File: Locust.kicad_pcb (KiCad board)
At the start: 2 copper layers, 133.3 x 44.4 mm, 12 parts, among them J1 Conn_01x03_MountingPin, J2 Conn_01x03_MountingPin, J3 Conn_01x03_MountingPin, J4 Conn_01x06_MountingPin, J5 Conn_01x12_MountingPin, J6 Conn_01x05_MountingPin, U1 DRV8847RTE, U2 DRV8847RTE, U3 nRF7002-QFXX, U4 ISP2053-AX, U5 AP63203WU, U6 AP63205WU

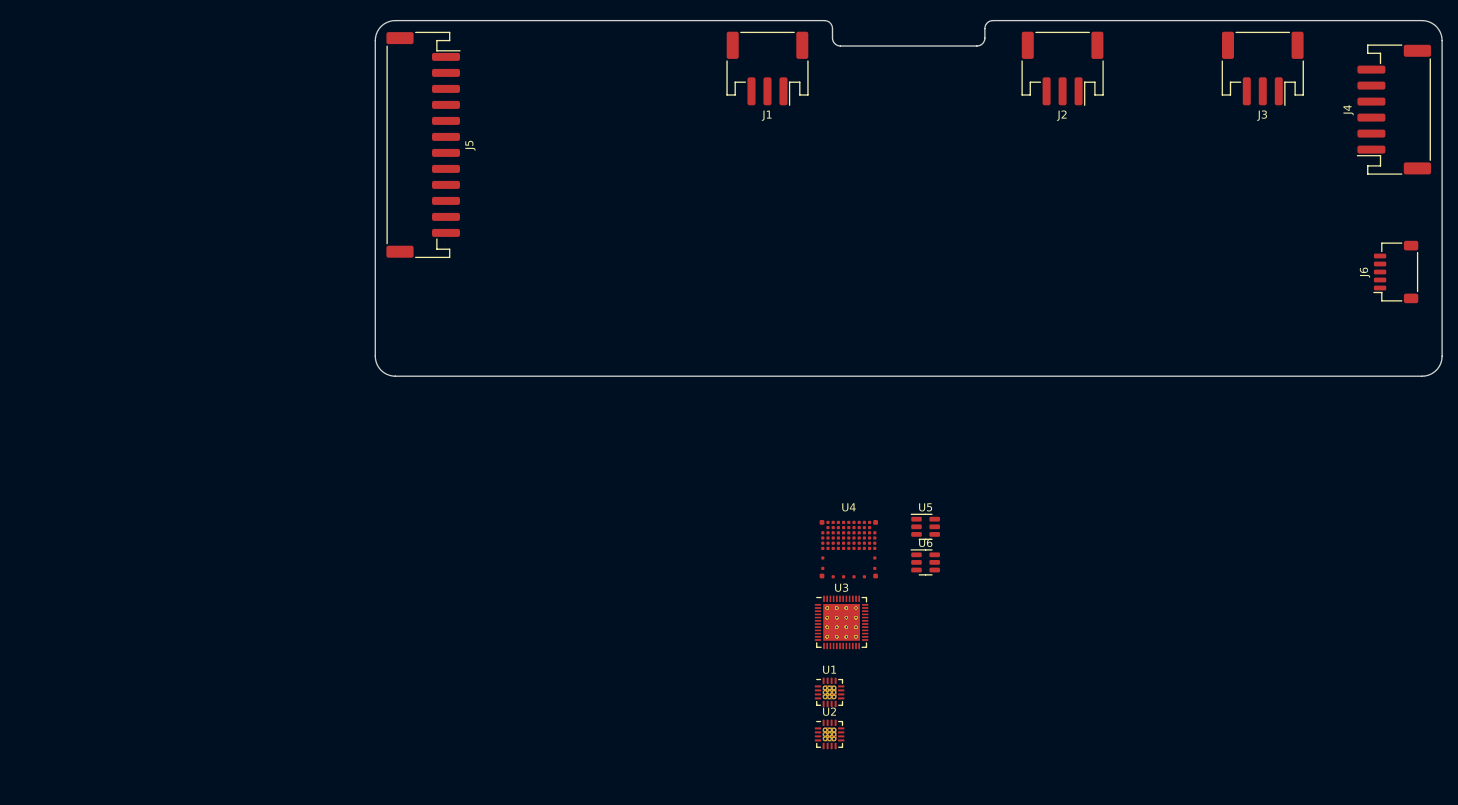
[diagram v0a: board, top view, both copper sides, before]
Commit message: Added nrf5340 and pi filters on output of switching supplies
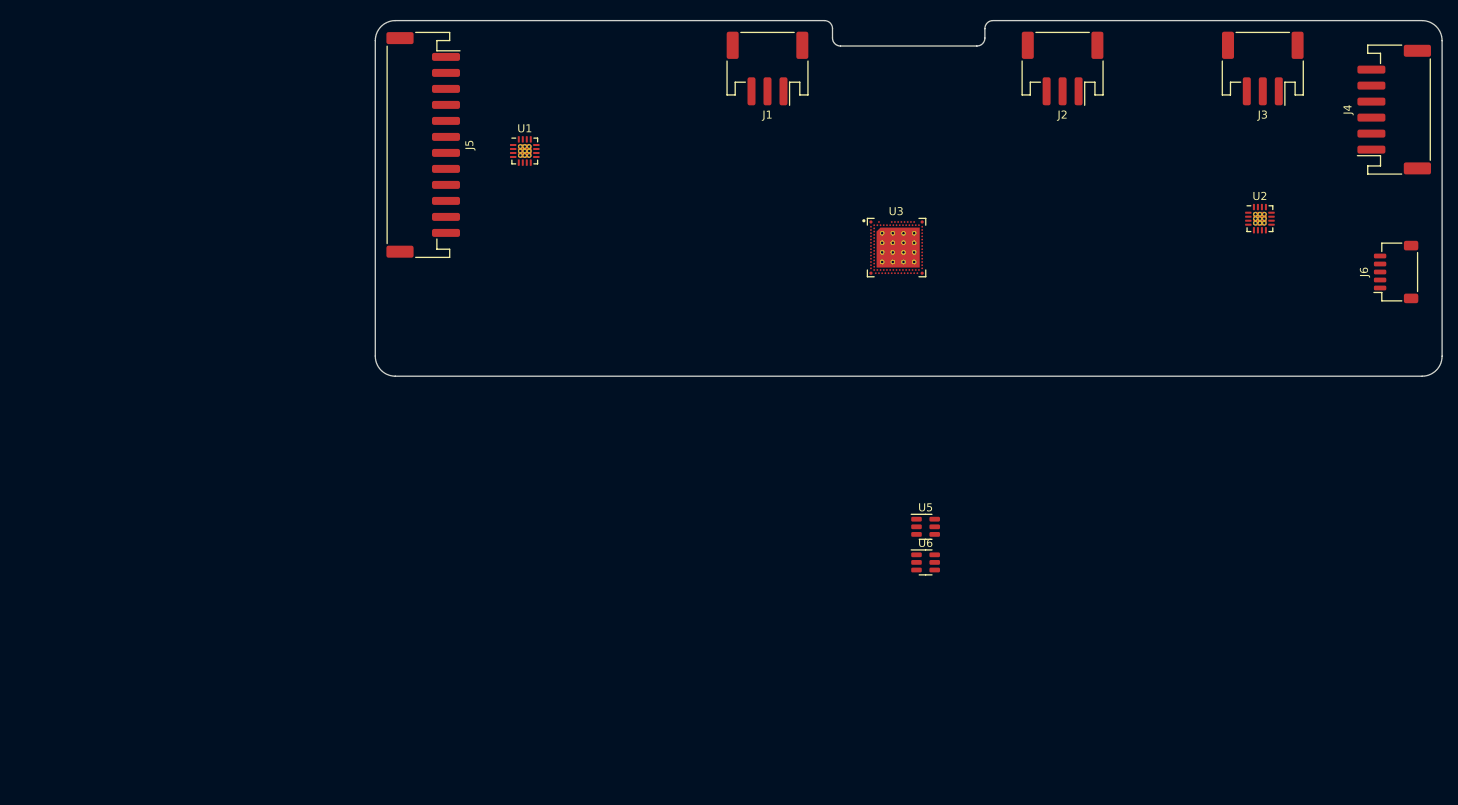
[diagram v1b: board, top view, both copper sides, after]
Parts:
- removed U4: ISP2053-AX, nordic-lib-kicad-nrf53-modules:ISP2053_8x8mm_LGA
- U3: value nRF7002-QFXX -> nRF5340-QKXX; footprint Package_DFN_QFN:QFN-48-1EP_6x6mm_P0.4mm_EP4.6x4.6mm_ThermalVias -> PCM_nordic-lib-kicad-nrf53:aQFN-94_7x7mm
- moved U2 84.0 mm to (175.7, 47.0)
- moved U1 77.7 mm to (83.8, 38.5)
- moved U3 47.5 mm to (130.2, 50.5)

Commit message: 10/09/23 - Schematic v0.1
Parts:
- added C34: 0.7p, Capacitor_SMD:C_0201_0603Metric, F.Cu at (174.1, 74.8)
- added C35: NC, Capacitor_SMD:C_0201_0603Metric, F.Cu at (174.1, 76.6)
- added C36: 1u, Inductor_SMD:L_0201_0603Metric, F.Cu at (174.1, 78.3)
- added H1: MountingHole_Pad, MountingHole:MountingHole_3.7mm_Pad, F.Cu at (88.1, 27.4)
- added H2: MountingHole_Pad, MountingHole:MountingHole_3.7mm_Pad, F.Cu at (86.9, 51.2)
- added H3: MountingHole_Pad, MountingHole:MountingHole_3.7mm_Pad, F.Cu at (148.8, 85.7)
- added H4: MountingHole_Pad, MountingHole:MountingHole_3.7mm_Pad, F.Cu at (184.5, 60.7)
- added J10: Conn_01x02, RF_Antenna:Texas_SWRA117D_2.4GHz_Left, F.Cu at (149.7, 59.3)
- added J7: Barrel_Jack_MountingPin, Connector_BarrelJack:BarrelJack_CUI_PJ-036AH-SMT_Horizontal, F.Cu at (28.6, 84.5)
- added J8: USB_C_Receptacle_USB2.0, Connector_USB:USB_C_Receptacle_HRO_TYPE-C-31-M-12, F.Cu at (113.1, 63.1)
- added J9: TC2030_SWD, PCM_marbastlib-various:CON_TC2030_outlined, B.Cu at (101.2, 48.8)
- added L5: 2.2n, Inductor_SMD:L_0201_0603Metric, F.Cu at (147.6, 57.8)
- added NT1: NetTie_2, NetTie:NetTie-2_SMD_Pad0.5mm, F.Cu at (63.0, 115.4)
- added NT2: NetTie_2, NetTie:NetTie-2_SMD_Pad0.5mm, F.Cu at (63.0, 116.9)
- added NT3: NetTie_2, NetTie:NetTie-2_SMD_Pad0.5mm, F.Cu at (90.0, 110.1)
- added NT4: NetTie_2, NetTie:NetTie-2_SMD_Pad0.5mm, F.Cu at (90.0, 111.6)
- added NT5: NetTie_2, NetTie:NetTie-2_SMD_Pad0.5mm, F.Cu at (90.0, 113.1)
- added R10: 100k, Resistor_SMD:R_0402_1005Metric, F.Cu at (181.7, 75.0)
- added R11: 100k, Resistor_SMD:R_0402_1005Metric, F.Cu at (181.7, 77.0)
- added R12: 100k, Resistor_SMD:R_0402_1005Metric, F.Cu at (181.7, 78.9)
- added R13: 100k, Resistor_SMD:R_0402_1005Metric, F.Cu at (181.7, 82.9)
- added R14: 100k, Resistor_SMD:R_0402_1005Metric, F.Cu at (181.7, 84.9)
- added R15: 100k, Resistor_SMD:R_0402_1005Metric, F.Cu at (181.7, 86.9)
- added R8: 5.1k, Resistor_SMD:R_0402_1005Metric, F.Cu at (176.7, 75.0)
- added R9: 5.1k, Resistor_SMD:R_0402_1005Metric, F.Cu at (176.7, 77.0)
- added TP1: UART_TX, TestPoint:TestPoint_Keystone_5015_Micro-Minature, B.Cu at (159.5, 51.2)
- added TP2: UART_RX, TestPoint:TestPoint_Keystone_5015_Micro-Minature, B.Cu at (153.6, 46.4)
- added U4: USBLC6-2SC6, Package_TO_SOT_SMD:SOT-23-6, F.Cu at (82.9, 116.6)
- added U7: MX25L3233FZN, Package_SON:WSON-8-1EP_6x5mm_P1.27mm_EP3.4x4mm, F.Cu at (127.1, 40.3)
- added Y1: 32MHz, Crystal:Crystal_SMD_2016-4Pin_2.0x1.6mm, F.Cu at (87.4, 116.2)
- added Y2: 32.768kHz, Crystal:Crystal_SMD_2012-2Pin_2.0x1.2mm, F.Cu at (74.5, 117.3)
- J1, J2, J3: value Conn_01x03_MountingPin -> JST PH S3B
- moved U5 20.6 mm to (115.5, 76.2)
- moved U3 19.2 mm to (149.4, 50.5)
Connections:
- J1 pad 2: unconnected-(J1-Pin_2-Pad2) -> /CutSheetSensors/PHOTO_EYE_LEFT
- J2 pad 2: unconnected-(J2-Pin_2-Pad2) -> /CutSheetSensors/EDGE_DETECTOR
- J3 pad 2: unconnected-(J3-Pin_2-Pad2) -> /CutSheetSensors/PHOTO_EYE_RIGHT
- U1 pad 12: unconnected-(U1-MODE-Pad12) -> /Motors_Encoders/MODE_2/3
- U1 pad 13: unconnected-(U1-IN2-Pad13) -> /Motors_Encoders/IN2_2/3
- U1 pad 14: unconnected-(U1-IN1-Pad14) -> /Motors_Encoders/IN1_2/3
- U1 pad 15: unconnected-(U1-~{SLEEP}-Pad15) -> /Motors_Encoders/~{SLEEP}_2/3
- U1 pad 6: unconnected-(U1-~{FAULT}-Pad6) -> /Motors_Encoders/~{FAULT}_2/3
- U1 pad 7: unconnected-(U1-IN3-Pad7) -> /Motors_Encoders/IN3_2/3
- U1 pad 8: unconnected-(U1-IN4-Pad8) -> /Motors_Encoders/IN4_2/3
- U1 pad 9: unconnected-(U1-TRQ-Pad9) -> /Motors_Encoders/TRQ_2/3
- U2 pad 12: unconnected-(U2-MODE-Pad12) -> /Motors_Encoders/MODE_1
- U2 pad 13: unconnected-(U2-IN2-Pad13) -> /Motors_Encoders/IN2_1
- U2 pad 14: unconnected-(U2-IN1-Pad14) -> /Motors_Encoders/IN1_1
- U2 pad 15: unconnected-(U2-~{SLEEP}-Pad15) -> /Motors_Encoders/~{SLEEP}_1
- U2 pad 6: unconnected-(U2-~{FAULT}-Pad6) -> /Motors_Encoders/~{FAULT}_1
- U2 pad 9: unconnected-(U2-TRQ-Pad9) -> /Motors_Encoders/TRQ_1
- U3 pad 104: unconnected-(U3B-VSS-Pad104) -> GND
- U3 pad A13: unconnected-(U3B-DECA-PadA13) -> Net-(U3B-DECA)
- U3 pad A15: unconnected-(U3B-DECD-PadA15) -> Net-(U3B-DECD)
- U3 pad A19: Net-(U3B-VDD-PadA19) -> Net-(U3B-VDDH)
- U3 pad A21: unconnected-(U3B-DCC-PadA21) -> Net-(U3B-DCC)
- U3 pad A23: unconnected-(U3B-DECN-PadA23) -> Net-(U3B-DECN)
- U3 pad A27: unconnected-(U3B-DECR-PadA27) -> Net-(U3B-DECR)
- U3 pad A5: unconnected-(U3B-VBUS-PadA5) -> Net-(U3B-VBUS)
- U3 pad AA31: unconnected-(U3A-SWDIO-PadAA31) -> /MCU/SWDIO
- U3 pad AC1: Net-(U3B-VDD-PadA19) -> Net-(U3B-VDDH)
- U3 pad AC31: unconnected-(U3A-~{RESET}-PadAC31) -> /MCU/~{RST}
- U3 pad AG1: Net-(U3B-VDD-PadA19) -> Net-(U3B-VDDH)
- U3 pad AJ31: Net-(U3B-VDD-PadA19) -> Net-(U3B-VDDH)
- U3 pad AK10: unconnected-(U3A-P0.15/IO2-PadAK10) -> Net-(U3A-P0.15/IO2)
- U3 pad AK12: unconnected-(U3A-P0.17/SCK-PadAK12) -> /MCU/SCK
- U3 pad AK14: unconnected-(U3A-P0.18/~{CS}-PadAK14) -> /MCU/~{CS}
- U3 pad AK16: unconnected-(U3A-P0.20-PadAK16) -> Net-(U3A-P0.20)
- U3 pad AK8: unconnected-(U3A-P0.14/IO1-PadAK8) -> Net-(U3A-P0.14/IO1)
- U3 pad AL11: Net-(U3B-VDD-PadA19) -> Net-(U3B-VDDH)
- U3 pad AL13: unconnected-(U3A-P0.19-PadAL13) -> Net-(U3A-P0.19)
- U3 pad AL17: Net-(U3B-VDD-PadA19) -> Net-(U3B-VDDH)
- U3 pad AL25: Net-(U3B-VDD-PadA19) -> Net-(U3B-VDDH)
- U3 pad AL3: Net-(U3B-VDD-PadA19) -> Net-(U3B-VDDH)
- U3 pad AL5: unconnected-(U3A-P0.13/IO0-PadAL5) -> Net-(U3A-P0.13/IO0)
- U3 pad AL7: Net-(U3B-VDD-PadA19) -> Net-(U3B-VDDH)
- U3 pad AL9: unconnected-(U3A-P0.16/IO3-PadAL9) -> Net-(U3A-P0.16/IO3)
- U3 pad B10: unconnected-(U3B-DCCD-PadB10) -> Net-(U3B-DCCD)
- U3 pad B2: unconnected-(U3A-D+-PadB2) -> /MCU/D+
- U3 pad B28: Net-(U3B-VDD-PadA19) -> Net-(U3B-VDDH)
- U3 pad B30: unconnected-(U3A-XC2-PadB30) -> Net-(U3A-XC2)
- U3 pad B4: unconnected-(U3A-D--PadB4) -> /MCU/D-
- U3 pad B6: unconnected-(U3B-DECUSB-PadB6) -> Net-(U3B-DECUSB)
- U3 pad B8: Net-(U3B-VDD-PadA19) -> Net-(U3B-VDDH)
- U3 pad C1: Net-(U3B-VDD-PadA19) -> Net-(U3B-VDDH)
- U3 pad C31: unconnected-(U3A-XC1-PadC31) -> Net-(U3A-XC1)
- U3 pad E1: unconnected-(U3B-VDDH-PadE1) -> Net-(U3B-VDDH)
- U3 pad E31: Net-(U3B-VDD-PadA19) -> Net-(U3B-VDDH)
- U3 pad G31: unconnected-(U3B-DECRF-PadG31) -> Net-(U3B-DECR)
- U3 pad L1: Net-(U3B-VDD-PadA19) -> Net-(U3B-VDDH)
- U3 pad L31: unconnected-(U3A-ANT-PadL31) -> Net-(U3A-ANT)
- U3 pad N1: unconnected-(U3A-P0.00/XL1-PadN1) -> Net-(U3A-P0.00/XL1)
- U3 pad N31: Net-(U3B-VDD-PadA19) -> Net-(U3B-VDDH)
- U3 pad R1: unconnected-(U3A-P0.01/XL2-PadR1) -> Net-(U3A-P0.01/XL2)
- U3 pad U1: Net-(U3B-VDD-PadA19) -> Net-(U3B-VDDH)
- U3 pad W31: unconnected-(U3A-SWDCLK-PadW31) -> /MCU/SWCLK
- U5 pad 1: +3.3V -> Net-(U5-FB)
- U6 pad 1: +5V -> Net-(U6-FB)
